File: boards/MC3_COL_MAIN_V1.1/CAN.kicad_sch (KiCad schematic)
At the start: 11 parts, among them J12 CAN, U8 TJA1051T/3

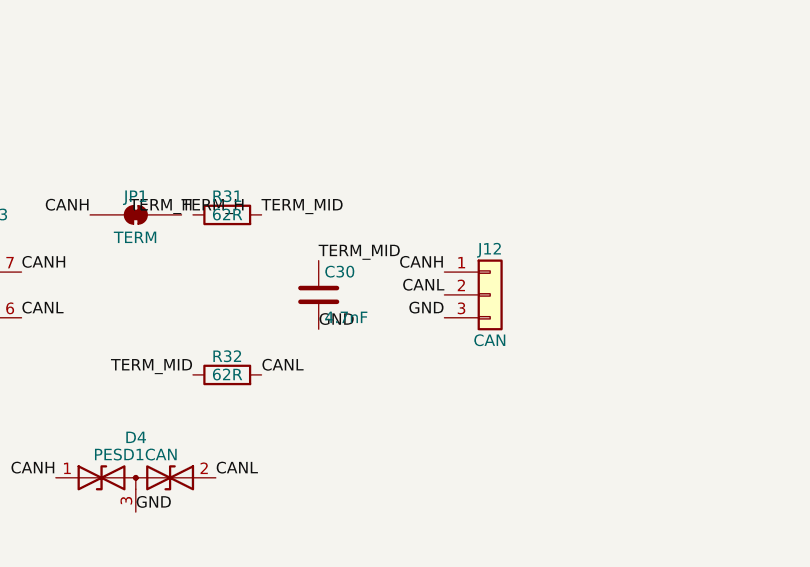
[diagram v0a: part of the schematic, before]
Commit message: V1.1: J13 machine-harness FFC (TE 84952-6, 1.0 mm 6-way) - YAW_OUT1/2 via new OUT1/OUT2 sheet pins, VIN_PAD/GND/CANH/CANL; ERC 0 errors
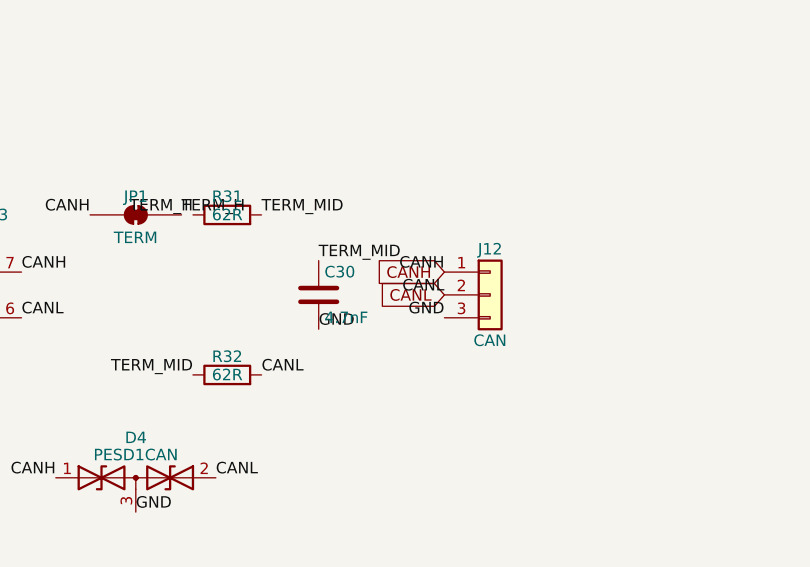
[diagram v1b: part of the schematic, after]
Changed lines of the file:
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@@
 	(generator_version "10.0")
 	(paper "A4")
-	(text "CAN - machine control link (decision 2026-08-22; vault Control Electronics open item). STM32F412 CAN1 (PA11 RX / PA12 TX) -> TJA1051T/3 -> split termination (2x62R + 4.7nF, solder-jumper JP70 bridged) + PESD1CAN -> pads CANH/CANL/GND. Classic CAN 500 kbit/s. Layout: CANH/CANL as a tight pair, transceiver and termination next to the pads, D70 nearest the pads."
-		(exclude_from_sim no)
-		(at 30 40 0)
-		(effects
-			(font
-				(size 1.5 1.5)
-			)
-		)
-	)
 	(wire
 		(pts
-			(xy 87.63 82.55) (xy 85.09 82.55)
+			(xy 87.63 82.55)
+			(xy 85.09 82.55)
 		)
 		(stroke
@@
 	(wire
 		(pts
-			(xy 87.63 77.47) (xy 85.09 77.47)
+			(xy 87.63 77.47)
+			(xy 85.09 77.47)
 		)
 		(stroke
@@
 	(wire
 		(pts
-			(xy 87.63 74.93) (xy 85.09 74.93)
+			(xy 87.63 74.93)
+			(xy 85.09 74.93)
 		)
 		(stroke
@@
 	(wire
 		(pts
-			(xy 60.96 57.15) (xy 60.96 54.61)
+			(xy 60.96 57.15)
+			(xy 60.96 54.61)
 		)
 		(stroke
@@
 		)
 	)
+	(text "CAN - machine control link (decision 2026-08-22; vault Control Electronics open item). STM32F412 CAN1 (PA11 RX / PA12 TX) -> TJA1051T/3 -> split termination (2x62R + 4.7nF, solder-jumper JP70 bridged) + PESD1CAN -> pads CANH/CANL/GND. Classic CAN 500 kbit/s. Layout: CANH/CANL as a tight pair, transceiver and termination next to the pads, D70 nearest the pads."
+		(at 30 40 0)
+		(effects
+			(font
+				(size 1.5 1.5)
+			)
+		)
+	)
 	(label "TERM_MID"
 		(at 139.7 71.12 0)
@@
 				)
 			)
+		)
+	)
+	(global_label "CANH"
+		(shape input)
+		(at 160.02 77.47 180)
+		(effects
+			(font
+				(size 1.27 1.27)
+			)
+			(justify right)
+		)
+	)
+	(global_label "CANL"
+		(shape input)
+		(at 160.02 80.01 180)
+		(effects
+			(font
+				(size 1.27 1.27)
+			)
+			(justify right)
 		)
 	)
@@
 		(at 135.89 88.9 90)
 		(unit 1)
-		(body_style 1)
 		(exclude_from_sim no)
 		(in_bom yes)
 		(on_board yes)
-		(in_pos_files yes)
 		(dnp no)
 		(property "Reference" "R32"
@@
 			)
 		)
+		(body_style 1)
+		(in_pos_files yes)
 		(pin "1"
 		)
@@
 		(at 165.1 80.01 0)
 		(unit 1)
-		(body_style 1)
 		(exclude_from_sim no)
 		(in_bom yes)
 		(on_board yes)
-		(in_pos_files yes)
 		(dnp no)
 		(property "Reference" "J12"
@@
 			)
 		)
+		(body_style 1)
+		(in_pos_files yes)
 		(pin "1"
 		)
@@
 		(at 71.12 106.68 0)
 		(unit 1)
-		(body_style 1)
 		(exclude_from_sim no)
 		(in_bom yes)
 		(on_board yes)
-		(in_pos_files yes)
 		(dnp no)
 		(property "Reference" "#PWR0120"
@@
 			)
 		)
+		(body_style 1)
+		(in_pos_files yes)
 		(pin "1"
 		)
@@
 		(at 71.12 66.04 0)
 		(unit 1)
-		(body_style 1)
 		(exclude_from_sim no)
 		(in_bom yes)
 		(on_board yes)
-		(in_pos_files yes)
 		(dnp no)
 		(property "Reference" "C28"
@@
 			)
 		)
+		(body_style 1)
+		(in_pos_files yes)
 		(pin "1"
 		)
@@
 		(at 125.73 100.33 0)
 		(unit 1)
-		(body_style 1)
 		(exclude_from_sim no)
 		(in_bom yes)
 		(on_board yes)
-		(in_pos_files yes)
 		(dnp no)
 		(property "Reference" "D4"
@@
 			)
 		)
+		(body_style 1)
+		(in_pos_files yes)
 		(pin "3"
 		)
@@
 		(at 78.74 66.04 0)
 		(unit 1)
-		(body_style 1)
 		(exclude_from_sim no)
 		(in_bom yes)
 		(on_board yes)
-		(in_pos_files yes)
 		(dnp no)
 		(property "Reference" "C29"
@@
 			)
 		)
+		(body_style 1)
+		(in_pos_files yes)
 		(pin "1"
 		)
@@
 		(at 71.12 114.3 0)
 		(unit 1)
-		(body_style 1)
 		(exclude_from_sim no)
 		(in_bom yes)
 		(on_board yes)
-		(in_pos_files yes)
 		(dnp no)
 		(property "Reference" "#PWR0121"
@@
 			)
 		)
+		(body_style 1)
+		(in_pos_files yes)
 		(pin "1"
 		)
@@
 		(at 71.12 110.49 0)
 		(unit 1)
-		(body_style 1)
 		(exclude_from_sim no)
 		(in_bom yes)
 		(on_board yes)
-		(in_pos_files yes)
 		(dnp no)
 		(property "Reference" "C43"
@@
 			)
 		)
+		(body_style 1)
+		(in_pos_files yes)
 		(pin "2"
 		)
@@
 		(at 125.73 71.12 0)
 		(unit 1)
-		(body_style 1)
 		(exclude_from_sim no)
 		(in_bom yes)
 		(on_board yes)
-		(in_pos_files yes)
 		(dnp no)
 		(property "Reference" "JP1"
@@
 			)
 		)
+		(body_style 1)
+		(in_pos_files yes)
 		(pin "1"
 		)
@@
 		(at 60.96 60.96 0)
 		(unit 1)
-		(body_style 1)
 		(exclude_from_sim no)
 		(in_bom yes)
 		(on_board yes)
-		(in_pos_files yes)
 		(dnp no)
 		(property "Reference" "FB3"
@@
 			)
 		)
+		(body_style 1)
+		(in_pos_files yes)
 		(pin "1"
 		)
@@
 		(at 135.89 71.12 90)
 		(unit 1)
-		(body_style 1)
 		(exclude_from_sim no)
 		(in_bom yes)
 		(on_board yes)
-		(in_pos_files yes)
 		(dnp no)
 		(property "Reference" "R31"
@@
 			)
 		)
+		(body_style 1)
+		(in_pos_files yes)
 		(pin "1"
 		)
@@
 		(at 146.05 80.01 0)
 		(unit 1)
-		(body_style 1)
 		(exclude_from_sim no)
 		(in_bom yes)
 		(on_board yes)
-		(in_pos_files yes)
 		(dnp no)
 		(property "Reference" "C30"
@@
 			)
 		)
+		(body_style 1)
+		(in_pos_files yes)
 		(pin "1"
 		)
@@
 		(at 100.33 90.17 0)
 		(unit 1)
-		(body_style 1)
 		(exclude_from_sim no)
 		(in_bom yes)
 		(on_board yes)
-		(in_pos_files yes)
 		(dnp no)
 		(property "Reference" "#PWR022"
@@
 			)
 		)
+		(body_style 1)
+		(in_pos_files yes)
 		(pin "1"
 		)
@@
 		(at 100.33 80.01 0)
 		(unit 1)
-		(body_style 1)
 		(exclude_from_sim no)
 		(in_bom yes)
 		(on_board yes)
-		(in_pos_files yes)
 		(dnp no)
 		(property "Reference" "U8"
@@
 			)
 		)
+		(body_style 1)
+		(in_pos_files yes)
 		(pin "1"
 		)
@@
 		(at 60.96 64.77 180)
 		(unit 1)
-		(body_style 1)
 		(exclude_from_sim no)
 		(in_bom yes)
 		(on_board yes)
-		(in_pos_files yes)
 		(dnp no)
 		(property "Reference" "#PWR021"
@@
 			)
 		)
+		(body_style 1)
+		(in_pos_files yes)
 		(pin "1"
 		)

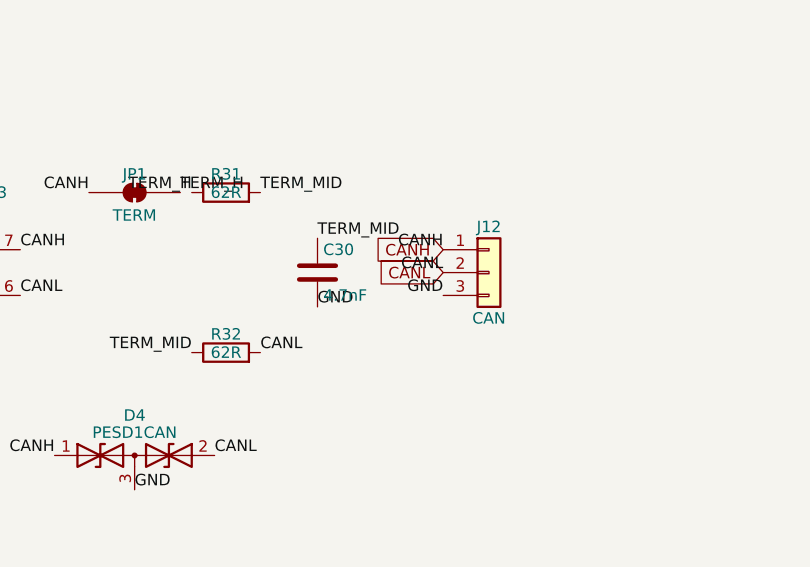
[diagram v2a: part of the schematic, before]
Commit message: V1.1: encoder FFC pin 4 -> RC_OUT_leafN (optical-fallback B channel over the open-drain ripple net); ERC 0 errors
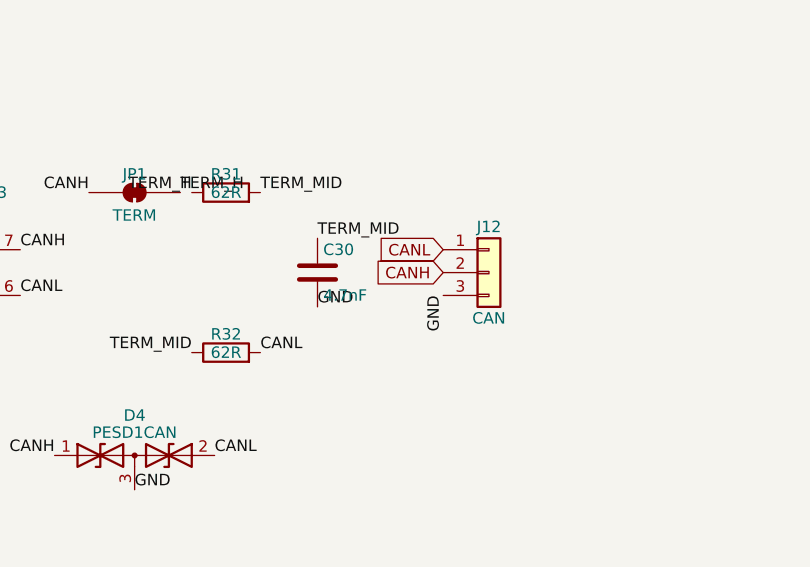
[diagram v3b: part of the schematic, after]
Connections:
- net CANH: now also J12.2 (Pin_2); no longer J12.1 (Pin_1)
- net CANL: now also J12.1 (Pin_1); no longer J12.2 (Pin_2)
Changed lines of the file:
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@@
-	)
-	(label "CANH"
-		(at 160.02 77.47 180)
-		(effects
-			(font
-				(size 1.27 1.27)
-			)
-			(justify right bottom)
-		)
 	)
 	(label "CANH"
@@
 	)
 	(label "GND"
-		(at 160.02 82.55 180)
-		(effects
-			(font
-				(size 1.27 1.27)
-			)
-			(justify right bottom)
-		)
-	)
-	(label "CANL"
-		(at 160.02 80.01 180)
+		(at 160.02 82.55 270)
 		(effects
 			(font
@@
 		)
 	)
-	(global_label "CANH"
+	(global_label "CANL"
 		(shape input)
 		(at 160.02 77.47 180)
@@
 		)
 	)
-	(global_label "CANL"
+	(global_label "CANH"
 		(shape input)
 		(at 160.02 80.01 180)
